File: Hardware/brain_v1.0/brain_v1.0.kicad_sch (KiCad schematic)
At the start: 80 parts, among them J1 Conn_01x02, J10 RFID, J11 Conn_01x04, J12 Conn_01x04, J13 Conn_01x02, J14 Conn_01x02, J15 Conn_01x05, J16 Conn_01x02, J2 Conn_01x02, J3 Conn_01x03, J4 JTAG, J5 Conn_01x02, J6 UART, J7 Conn_01x03, J8 UART Backup, J9 Conn_01x02, Q1 BSS138, Q2 BSS138, Q3 SMD-TRANSISTORS-NPN-25V-500MW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, Q4 SMD-TRANSISTORS-NPN-25V-500MW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, Q5 BSS138, Q6 BSS138, SW1 SW_Push, SW2 SW_Push, U1 ESP32-WROOM-32E 4MB, U2 NAU7802SGI

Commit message: Halfway done with the brain layout--had to fix some issues from the schematic and relink designators. I also added an md file in the Hardware library that specifies how someone can link the Solar Car library and our 3rd party parts (I added both of those folders as well).
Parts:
- removed TP6, TP7: TestPoint, TestPoint:TestPoint_Keystone_5010-5014_Multipurpose, symbol Connector:TestPoint
- added D1, D2: LED, LED_SMD:LED_0603_1608Metric, symbol device:LED
- added Q7: SMD-TRANSISTORS-NPN-25V-500MW_SOT-23_, S8050:S8050-SMD, symbol S8050-SMD:SMD-TRANSISTORS-NPN-25V-500MW_SOT-23_
- added R27, R28: 330, Resistor_SMD:R_0603_1608Metric, symbol Device:R_US
- renumbered D1 to D3, D2 to D4, J15 to J11, J13 to J12, J14 to J13, J16 to J14, J11 to J15, J12 to J16, R14 to R13, R15 to R14, R16 to R15, R13 to R16, R27 to R29, R28 to R30, R29 to R31, R30 to R32, R31 to R33, R7 to R6, R8 to R7, R9 to R8, R6 to R9
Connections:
- net +3V3: now also R28.1
- net GND: now also Q7.2, R27.2
- net GPIO0: now also Q7.1
- net GPIO21: now also J11.1 (Pin_1); no longer J11.5 (Pin_5)
- net GPIO25: now also J11.3 (Pin_3); no longer J11.4 (Pin_4)
- net GPIO27: now also J11.2 (Pin_2); no longer J11.3 (Pin_3)
- net GPIO32: now also J11.5 (Pin_5); no longer J11.2 (Pin_2)
- net GPIO33: now also J11.4 (Pin_4); no longer J11.1 (Pin_1)
- net MCU_Power: now also D1.2 (A)
- new net: D2.1 (K), Q7.3
- new net: D2.2 (A), R28.2
- new net: D1.1 (K), R27.1
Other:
- note added: "Status LEDs"

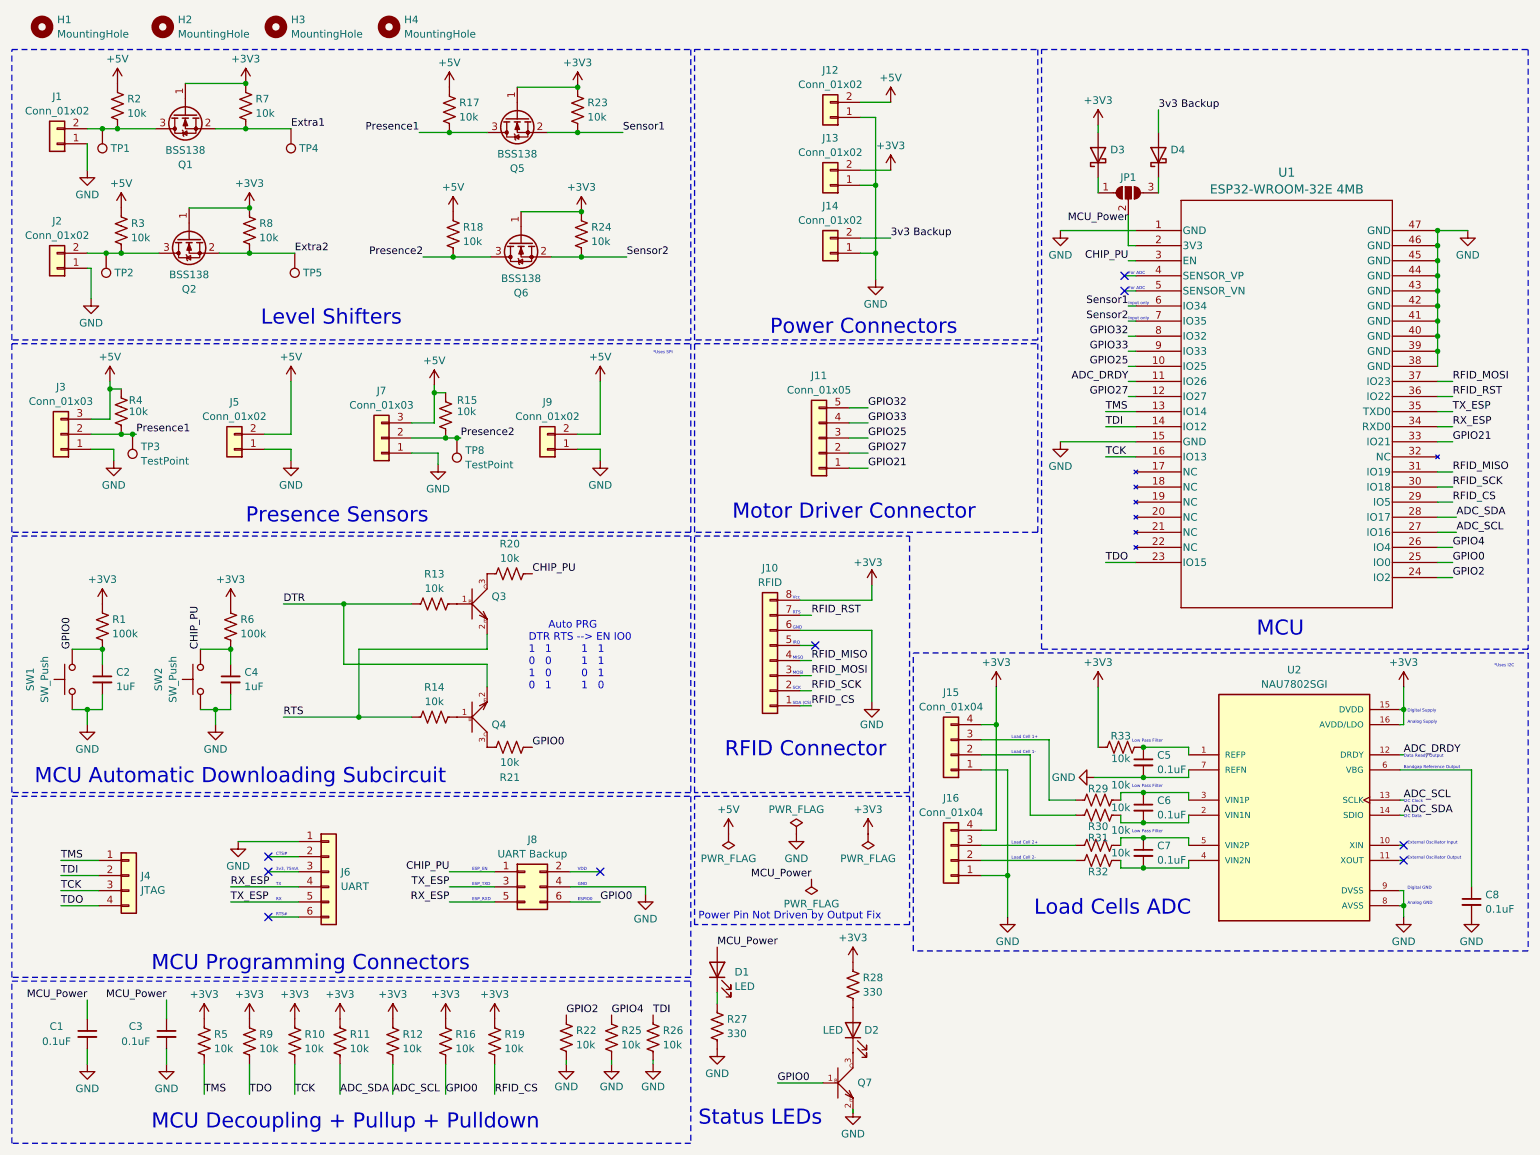
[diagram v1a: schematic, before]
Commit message: more than halfway done with brain, optimizing routing
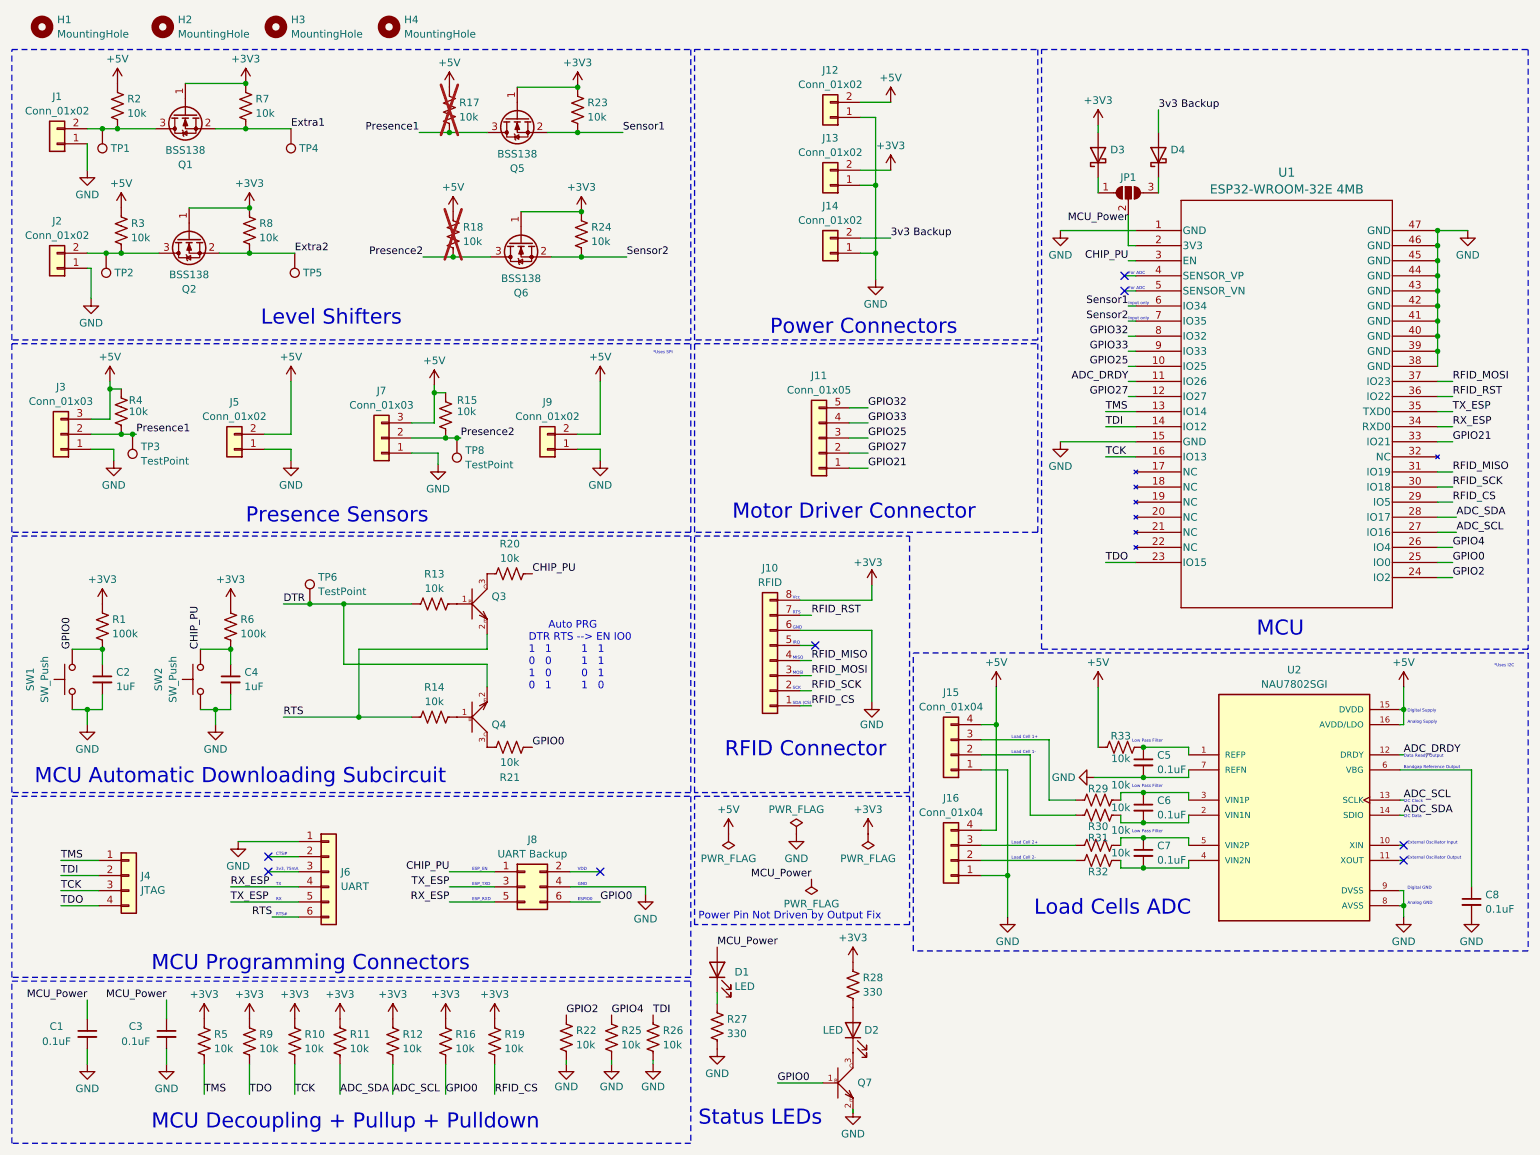
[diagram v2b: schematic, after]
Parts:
- added TP6: TestPoint, TestPoint:TestPoint_Keystone_5010-5014_Multipurpose, symbol Connector:TestPoint
- R17, R18: now not fitted
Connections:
- net +3V3: no longer J15.4 (Pin_4), J16.4 (Pin_4), R33.1, U2.15 (DVDD), U2.16 (AVDD/LDO)
- net +5V: now also J15.4 (Pin_4), J16.4 (Pin_4), R33.1, U2.15 (DVDD), U2.16 (AVDD/LDO)
- net DTR: now also TP6.1
- net RTS: now also J6.6 (Pin_6)
- no-connect marks 9 -> 8
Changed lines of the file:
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@@
   (title_block
     (title "Brain Board")
-    (date "2025-03-10")
+    (date "2025-03-11")
     (rev "1.0")
     (company "ECE 445: Senior Capstone Project")
@@
   (junction (at 179.705 158.75) (diameter 0) (color 0 0 0 0)
   )
+  (junction (at 62.23 113.03) (diameter 0) (color 0 0 0 0)
+  )
   (junction (at 107.315 33.655) (diameter 0) (color 0 0 0 0)
   )
@@
   (no_connect (at 55.245 158.115))
   (no_connect (at 199.39 57.785))
-  (no_connect (at 55.245 165.735))
   (no_connect (at 111.125 158.115))
   (no_connect (at 199.39 60.325))
@@
     (stroke (width 0) (type default))
   )
+  (wire (pts (xy 62.23 113.03) (xy 67.945 113.03))
+    (stroke (width 0) (type default))
+  )
   (wire (pts (xy 200.025 65.405) (xy 201.295 65.405))
     (stroke (width 0) (type default))
@@
     (stroke (width 0) (type default))
   )
-  (wire (pts (xy 57.785 113.03) (xy 67.945 113.03))
+  (wire (pts (xy 57.785 113.03) (xy 62.23 113.03))
     (stroke (width 0) (type default))
   )
@@
     (stroke (width 0) (type default))
   )
-  (wire (pts (xy 55.245 165.735) (xy 60.325 165.735))
-    (stroke (width 0) (type default))
-  )
   (wire (pts (xy 111.125 84.455) (xy 107.315 84.455))
     (stroke (width 0) (type default))
@@
     (stroke (width 0) (type default))
   )
+  (wire (pts (xy 55.88 165.735) (xy 60.325 165.735))
+    (stroke (width 0) (type default))
+  )
   (wire (pts (xy 202.565 144.78) (xy 210.185 144.78))
     (stroke (width 0) (type default))
@@
     (effects (font (size 1.27 1.27)) (justify left bottom))
   )
+  (label "RTS" (at 55.88 165.735 180) (fields_autoplaced)
+    (effects (font (size 1.27 1.27)) (justify right bottom))
+  )
   (label "MCU_Power" (at 200.025 48.895 180) (fields_autoplaced)
     (effects (font (size 1.27 1.27)) (justify right bottom))
@@
     )
   )
+  (symbol (lib_id "Connector:TestPoint") (at 62.23 113.03 0) (unit 1)
+    (in_bom yes) (on_board yes) (dnp no) (fields_autoplaced)
+    (property "Reference" "TP6" (at 63.627 108.5159 0)
+      (effects (font (size 1.27 1.27)) (justify left))
+    )
+    (property "Value" "TestPoint" (at 63.627 110.9401 0)
+      (effects (font (size 1.27 1.27)) (justify left))
+    )
+    (property "Footprint" "TestPoint:TestPoint_Keystone_5010-5014_Multipurpose" (at 67.31 113.03 0)
+      (effects (font (size 1.27 1.27)) hide)
+    )
+    (property "Datasheet" "~" (at 67.31 113.03 0)
+      (effects (font (size 1.27 1.27)) hide)
+    )
+    (property "Link" "https://www.digikey.com/en/products/detail/keystone-electronics/5011/255333" (at 62.23 113.03 0)
+      (effects (font (size 1.27 1.27)) hide)
+    )
+    (property "MPN" "36-5011-ND" (at 62.23 113.03 0)
+      (effects (font (size 1.27 1.27)) hide)
+    )
+    (pin "1")
+    (instances
+      (project "brain_v1.0"
+        (path "/1e1b062d-fad0-427c-a622-c5b8a80b5268"
+          (reference "TP6") (unit 1)
+        )
+      )
+    )
+  )
   (symbol (lib_id "Connector_Generic:Conn_01x02") (at 149.86 42.545 180) (unit 1)
     (in_bom yes) (on_board yes) (dnp no) (fields_autoplaced)
@@
     )
   )
-  (symbol (lib_id "power:+3V3") (at 194.945 127 0) (unit 1)
-    (in_bom yes) (on_board yes) (dnp no) (fields_autoplaced)
-    (property "Reference" "#PWR054" (at 194.945 130.81 0)
-      (effects (font (size 1.27 1.27)) hide)
-    )
-    (property "Value" "+3V3" (at 194.945 122.8669 0)
-      (effects (font (size 1.27 1.27)))
-    )
-    (property "Footprint" "" (at 194.945 127 0)
-      (effects (font (size 1.27 1.27)) hide)
-    )
-    (property "Datasheet" "" (at 194.945 127 0)
-      (effects (font (size 1.27 1.27)) hide)
-    )
-    (pin "1")
-    (instances
-      (project "brain_v1.0"
-        (path "/1e1b062d-fad0-427c-a622-c5b8a80b5268"
-          (reference "#PWR054") (unit 1)
-        )
-      )
-    )
-  )
   (symbol (lib_id "Device:C_Small") (at 202.565 139.7 0) (unit 1)
     (in_bom yes) (on_board yes) (dnp no) (fields_autoplaced)
@@
     )
   )
-  (symbol (lib_id "power:+3V3") (at 246.38 127 0) (unit 1)
-    (in_bom yes) (on_board yes) (dnp no) (fields_autoplaced)
-    (property "Reference" "#PWR055" (at 246.38 130.81 0)
-      (effects (font (size 1.27 1.27)) hide)
-    )
-    (property "Value" "+3V3" (at 246.38 122.8669 0)
-      (effects (font (size 1.27 1.27)))
-    )
-    (property "Footprint" "" (at 246.38 127 0)
-      (effects (font (size 1.27 1.27)) hide)
-    )
-    (property "Datasheet" "" (at 246.38 127 0)
-      (effects (font (size 1.27 1.27)) hide)
-    )
-    (pin "1")
-    (instances
-      (project "brain_v1.0"
-        (path "/1e1b062d-fad0-427c-a622-c5b8a80b5268"
-          (reference "#PWR055") (unit 1)
-        )
-      )
-    )
-  )
   (symbol (lib_id "Connector:TestPoint") (at 86.995 85.09 180) (unit 1)
     (in_bom yes) (on_board yes) (dnp no) (fields_autoplaced)
@@
     )
   )
+  (symbol (lib_id "power:+5V") (at 177.8 127 0) (unit 1)
+    (in_bom yes) (on_board yes) (dnp no) (fields_autoplaced)
+    (property "Reference" "#PWR048" (at 177.8 130.81 0)
+      (effects (font (size 1.27 1.27)) hide)
+    )
+    (property "Value" "+5V" (at 177.8 122.8669 0)
+      (effects (font (size 1.27 1.27)))
+    )
+    (property "Footprint" "" (at 177.8 127 0)
+      (effects (font (size 1.27 1.27)) hide)
+    )
+    (property "Datasheet" "" (at 177.8 127 0)
+      (effects (font (size 1.27 1.27)) hide)
+    )
+    (pin "1")
+    (instances
+      (project "brain_v1.0"
+        (path "/1e1b062d-fad0-427c-a622-c5b8a80b5268"
+          (reference "#PWR048") (unit 1)
+        )
+      )
+    )
+  )
   (symbol (lib_id "power:GND") (at 144.145 151.765 0) (unit 1)
     (in_bom yes) (on_board yes) (dnp no) (fields_autoplaced)
@@
     )
   )
-  (symbol (lib_id "power:+3V3") (at 177.8 127 0) (unit 1)
-    (in_bom yes) (on_board yes) (dnp no) (fields_autoplaced)
-    (property "Reference" "#PWR048" (at 177.8 130.81 0)
-      (effects (font (size 1.27 1.27)) hide)
-    )
-    (property "Value" "+3V3" (at 177.8 122.8669 0)
-      (effects (font (size 1.27 1.27)))
-    )
-    (property "Footprint" "" (at 177.8 127 0)
-      (effects (font (size 1.27 1.27)) hide)
-    )
-    (property "Datasheet" "" (at 177.8 127 0)
-      (effects (font (size 1.27 1.27)) hide)
-    )
-    (pin "1")
-    (instances
-      (project "brain_v1.0"
-        (path "/1e1b062d-fad0-427c-a622-c5b8a80b5268"
-          (reference "#PWR048") (unit 1)
-        )
-      )
-    )
-  )
   (symbol (lib_id "power:+3V3") (at 107.315 26.035 0) (unit 1)
     (in_bom yes) (on_board yes) (dnp no) (fields_autoplaced)
@@
     )
   )
+  (symbol (lib_id "power:+5V") (at 194.945 127 0) (unit 1)
+    (in_bom yes) (on_board yes) (dnp no) (fields_autoplaced)
+    (property "Reference" "#PWR054" (at 194.945 130.81 0)
+      (effects (font (size 1.27 1.27)) hide)
+    )
+    (property "Value" "+5V" (at 194.945 122.8669 0)
+      (effects (font (size 1.27 1.27)))
+    )
+    (property "Footprint" "" (at 194.945 127 0)
+      (effects (font (size 1.27 1.27)) hide)
+    )
+    (property "Datasheet" "" (at 194.945 127 0)
+      (effects (font (size 1.27 1.27)) hide)
+    )
+    (pin "1")
+    (instances
+      (project "brain_v1.0"
+        (path "/1e1b062d-fad0-427c-a622-c5b8a80b5268"
+          (reference "#PWR054") (unit 1)
+        )
+      )
+    )
+  )
   (symbol (lib_id "Connector_Generic:Conn_01x02") (at 19.685 56.515 180) (unit 1)
     (in_bom yes) (on_board yes) (dnp no) (fields_autoplaced)
@@
   )
   (symbol (lib_id "device:R_US") (at 86.36 50.8 0) (unit 1)
-    (in_bom yes) (on_board yes) (dnp no) (fields_autoplaced)
+    (in_bom yes) (on_board yes) (dnp yes) (fields_autoplaced)
     (property "Reference" "R18" (at 88.011 49.5879 0)
       (effects (font (size 1.27 1.27)) (justify left))
@@
     )
   )
+  (symbol (lib_id "power:+5V") (at 246.38 127 0) (unit 1)
+    (in_bom yes) (on_board yes) (dnp no) (fields_autoplaced)
+    (property "Reference" "#PWR055" (at 246.38 130.81 0)
+      (effects (font (size 1.27 1.27)) hide)
+    )
+    (property "Value" "+5V" (at 246.38 122.8669 0)
+      (effects (font (size 1.27 1.27)))
+    )
+    (property "Footprint" "" (at 246.38 127 0)
+      (effects (font (size 1.27 1.27)) hide)
+    )
+    (property "Datasheet" "" (at 246.38 127 0)
+      (effects (font (size 1.27 1.27)) hide)
+    )
+    (pin "1")
+    (instances
+      (project "brain_v1.0"
+        (path "/1e1b062d-fad0-427c-a622-c5b8a80b5268"
+          (reference "#PWR055") (unit 1)
+        )
+      )
+    )
+  )
   (symbol (lib_id "device:R_US") (at 30.48 50.165 0) (unit 1)
     (in_bom yes) (on_board yes) (dnp no) (fields_autoplaced)
@@
   )
   (symbol (lib_id "device:R_US") (at 85.725 29.845 0) (unit 1)
-    (in_bom yes) (on_board yes) (dnp no) (fields_autoplaced)
+    (in_bom yes) (on_board yes) (dnp yes) (fields_autoplaced)
     (property "Reference" "R17" (at 87.376 28.6329 0)
       (effects (font (size 1.27 1.27)) (justify left))

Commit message: brain done! except for stitching vias
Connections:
- net ADC_DRDY: now also U1.33 (IO21); no longer U1.11 (IO26)
- net GPIO27: now also J11.1 (Pin_1); no longer J11.2 (Pin_2)
- removed net GPIO21: J11.1 (Pin_1), U1.33 (IO21)
- new net GPIO26: J11.2 (Pin_2), U1.11 (IO26)
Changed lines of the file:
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@@
     (effects (font (size 1.27 1.27)) (justify left bottom))
   )
-  (label "GPIO27" (at 156.21 87.63 0) (fields_autoplaced)
+  (label "GPIO27" (at 156.21 90.17 0) (fields_autoplaced)
     (effects (font (size 1.27 1.27)) (justify left bottom))
   )
@@
     (effects (font (size 1.27 1.27)) (justify left bottom))
   )
-  (label "GPIO21" (at 254.635 85.725 0) (fields_autoplaced)
-    (effects (font (size 1.27 1.27)) (justify left bottom))
+  (label "GPIO26" (at 200.025 75.565 180) (fields_autoplaced)
+    (effects (font (size 1.27 1.27)) (justify right bottom))
   )
   (label "Sensor2" (at 115.57 54.61 0) (fields_autoplaced)
@@
     (effects (font (size 1.27 1.27)) (justify right bottom))
   )
-  (label "ADC_DRDY" (at 200.025 75.565 180) (fields_autoplaced)
-    (effects (font (size 1.27 1.27)) (justify right bottom))
+  (label "ADC_DRDY" (at 254.635 85.725 0) (fields_autoplaced)
+    (effects (font (size 1.27 1.27)) (justify left bottom))
   )
   (label "TDI" (at 120.015 182.245 0) (fields_autoplaced)
@@
     (effects (font (size 1.27 1.27)) (justify right bottom))
   )
-  (label "GPIO21" (at 156.21 90.17 0) (fields_autoplaced)
+  (label "GPIO26" (at 156.21 87.63 0) (fields_autoplaced)
     (effects (font (size 1.27 1.27)) (justify left bottom))
   )
